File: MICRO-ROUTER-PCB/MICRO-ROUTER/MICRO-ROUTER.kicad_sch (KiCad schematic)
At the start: 71 parts, among them J2 USB_A, J3 USB_C_Receptacle_USB2.0_16P, J4 Battery Connector, J5 SPI Header, J6 GPIO Header, J7 RJ45 5-2301996-6, Q1 FS8205A, SW2 8Devices Reset, SW3 UART Reset, U1 TP4056, U2 XC9142B33DMR-G, U3 CP2102N-Axx-xQFN20, U4 DW01A, X1 142-0711-821

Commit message: -added extra charge LED -wired TP4056
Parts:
- added D3: LED Green, LED_SMD:LED_0603_1608Metric, symbol Device:LED
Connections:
- net at C4.2, D1.2 (A), D2.2 (A)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: now also D3.2 (A)
- net at D2.1 (K), R5.1: now also D3.1 (K)
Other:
- moved on the sheet: C4, D2
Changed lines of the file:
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@@
 	)
 	(junction
-		(at 146.05 110.49)
-		(diameter 0)
-		(color 0 0 0 0)
-	)
-	(junction
 		(at 133.35 110.49)
 		(diameter 0)
@@
 	)
 	(junction
+		(at 160.02 110.49)
+		(diameter 0)
+		(color 0 0 0 0)
+	)
+	(junction
 		(at 212.09 81.28)
 		(diameter 0)
@@
 	)
 	(junction
+		(at 151.13 93.98)
+		(diameter 0)
+		(color 0 0 0 0)
+	)
+	(junction
 		(at 180.34 212.09)
 		(diameter 0)
@@
 	)
 	(junction
+		(at 151.13 110.49)
+		(diameter 0)
+		(color 0 0 0 0)
+	)
+	(junction
 		(at 314.96 60.96)
 		(diameter 0)
@@
 	(wire
 		(pts
+			(xy 151.13 93.98) (xy 151.13 99.06)
+		)
+		(stroke
+			(width 0)
+			(type default)
+		)
+	)
+	(wire
+		(pts
 			(xy 323.85 113.03) (xy 326.39 113.03)
 		)
@@
 	(wire
 		(pts
-			(xy 146.05 99.06) (xy 146.05 93.98)
+			(xy 160.02 99.06) (xy 160.02 93.98)
 		)
 		(stroke
@@
 	(wire
 		(pts
+			(xy 151.13 93.98) (xy 160.02 93.98)
+		)
+		(stroke
+			(width 0)
+			(type default)
+		)
+	)
+	(wire
+		(pts
 			(xy 115.57 72.39) (xy 114.3 72.39)
 		)
@@
 	(wire
 		(pts
+			(xy 161.29 110.49) (xy 160.02 110.49)
+		)
+		(stroke
+			(width 0)
+			(type default)
+		)
+	)
+	(wire
+		(pts
 			(xy 99.06 83.82) (xy 102.87 83.82)
 		)
@@
 	(wire
 		(pts
+			(xy 151.13 93.98) (xy 146.05 93.98)
+		)
+		(stroke
+			(width 0)
+			(type default)
+		)
+	)
+	(wire
+		(pts
 			(xy 274.32 187.96) (xy 295.91 187.96)
 		)
@@
 	(wire
 		(pts
+			(xy 151.13 106.68) (xy 151.13 110.49)
+		)
+		(stroke
+			(width 0)
+			(type default)
+		)
+	)
+	(wire
+		(pts
 			(xy 171.45 219.71) (xy 190.5 219.71)
 		)
@@
 	(wire
 		(pts
-			(xy 146.05 106.68) (xy 146.05 110.49)
+			(xy 160.02 106.68) (xy 160.02 110.49)
 		)
 		(stroke
@@
 	(wire
 		(pts
-			(xy 146.05 110.49) (xy 139.7 110.49)
+			(xy 139.7 110.49) (xy 151.13 110.49)
 		)
 		(stroke
@@
 	(wire
 		(pts
+			(xy 151.13 110.49) (xy 160.02 110.49)
+		)
+		(stroke
+			(width 0)
+			(type default)
+		)
+	)
+	(wire
+		(pts
 			(xy 306.07 60.96) (xy 314.96 60.96)
 		)
@@
 	(symbol
 		(lib_id "power:GND")
-		(at 153.67 110.49 180)
+		(at 168.91 110.49 180)
 		(unit 1)
 		(exclude_from_sim no)
@@
 		(fields_autoplaced yes)
 		(property "Reference" "#PWR028"
-			(at 153.67 104.14 0)
+			(at 168.91 104.14 0)
 			(effects
 				(font
@@
 		)
 		(property "Value" "GND"
-			(at 153.67 105.41 0)
+			(at 168.91 105.41 0)
 			(effects
 				(font
@@
 		)
 		(property "Footprint" ""
-			(at 153.67 110.49 0)
+			(at 168.91 110.49 0)
 			(effects
 				(font
@@
 		)
 		(property "Datasheet" ""
-			(at 153.67 110.49 0)
+			(at 168.91 110.49 0)
 			(effects
 				(font
@@
 		)
 		(property "Description" "Power symbol creates a global label with name \"GND\" , ground"
-			(at 153.67 110.49 0)
+			(at 168.91 110.49 0)
 			(effects
 				(font
@@
 	)
 	(symbol
+		(lib_id "Device:LED")
+		(at 151.13 102.87 270)
+		(unit 1)
+		(exclude_from_sim no)
+		(in_bom yes)
+		(on_board yes)
+		(dnp no)
+		(property "Reference" "D3"
+			(at 150.876 105.664 90)
+			(effects
+				(font
+					(size 1.27 1.27)
+				)
+				(justify right)
+			)
+		)
+		(property "Value" "LED Green"
+			(at 153.924 105.918 0)
+			(effects
+				(font
+					(size 1.27 1.27)
+				)
+				(justify right)
+			)
+		)
+		(property "Footprint" "LED_SMD:LED_0603_1608Metric"
+			(at 151.13 102.87 0)
+			(effects
+				(font
+					(size 1.27 1.27)
+				)
+				(hide yes)
+			)
+		)
+		(property "Datasheet" "~"
+			(at 151.13 102.87 0)
+			(effects
+				(font
+					(size 1.27 1.27)
+				)
+				(hide yes)
+			)
+		)
+		(property "Description" "Light emitting diode"
+			(at 151.13 102.87 0)
+			(effects
+				(font
+					(size 1.27 1.27)
+				)
+				(hide yes)
+			)
+		)
+		(pin "1"
+		)
+		(pin "2"
+		)
+		(instances
+			(project "MICRO-ROUTER"
+				(path "/ebd99a91-a0ff-4b6f-9899-bd1b2d3fbcb2"
+					(reference "D3")
+					(unit 1)
+				)
+			)
+		)
+	)
+	(symbol
 		(lib_id "Device:R")
 		(at 146.05 90.17 180)
@@
 	(symbol
 		(lib_id "Device:C")
-		(at 149.86 110.49 270)
+		(at 165.1 110.49 270)
 		(unit 1)
 		(exclude_from_sim no)
@@
 		(dnp no)
 		(property "Reference" "C4"
-			(at 150.114 114.046 90)
+			(at 165.354 114.046 90)
 			(effects
 				(font
@@
 		)
 		(property "Value" "100nf"
-			(at 149.86 116.332 90)
+			(at 165.1 116.332 90)
 			(effects
 				(font
@@
 		)
 		(property "Footprint" "Capacitor_SMD:C_0603_1608Metric"
-			(at 146.05 111.4552 0)
+			(at 161.29 111.4552 0)
 			(effects
 				(font
@@
 		)
 		(property "Datasheet" "~"
-			(at 149.86 110.49 0)
+			(at 165.1 110.49 0)
 			(effects
 				(font
@@
 		)
 		(property "Description" "Unpolarized capacitor"
-			(at 149.86 110.49 0)
+			(at 165.1 110.49 0)
 			(effects
 				(font
@@
 	(symbol
 		(lib_id "Device:LED")
-		(at 146.05 102.87 270)
+		(at 160.02 102.87 270)
 		(unit 1)
 		(exclude_from_sim no)
@@
 		(dnp no)
 		(property "Reference" "D2"
-			(at 145.796 105.664 90)
+			(at 159.766 105.664 90)
 			(effects
 				(font
@@
 		)
 		(property "Value" "LED Green"
-			(at 148.844 105.918 0)
+			(at 162.814 105.918 0)
 			(effects
 				(font
@@
 		)
 		(property "Footprint" "LED_SMD:LED_0603_1608Metric"
-			(at 146.05 102.87 0)
+			(at 160.02 102.87 0)
 			(effects
 				(font
@@
 		)
 		(property "Datasheet" "~"
-			(at 146.05 102.87 0)
+			(at 160.02 102.87 0)
 			(effects
 				(font
@@
 		)
 		(property "Description" "Light emitting diode"
-			(at 146.05 102.87 0)
+			(at 160.02 102.87 0)
 			(effects
 				(font

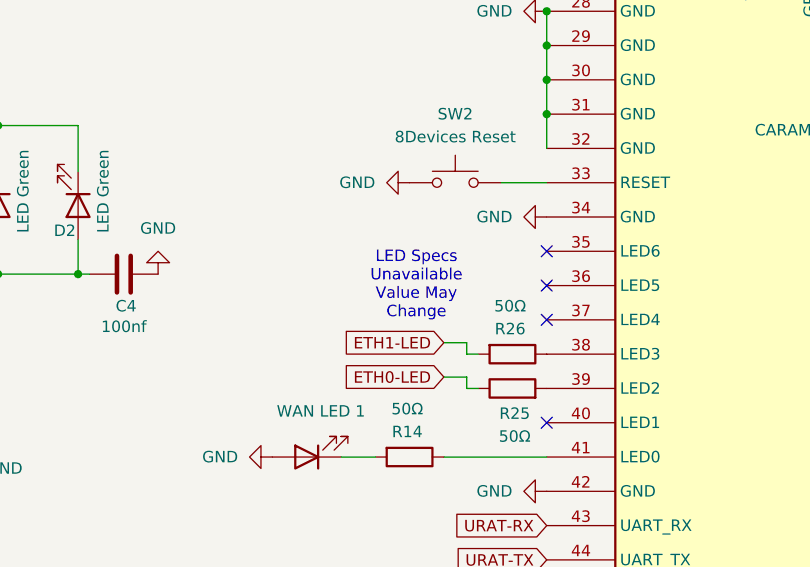
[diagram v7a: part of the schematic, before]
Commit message: -Wired up Mofset
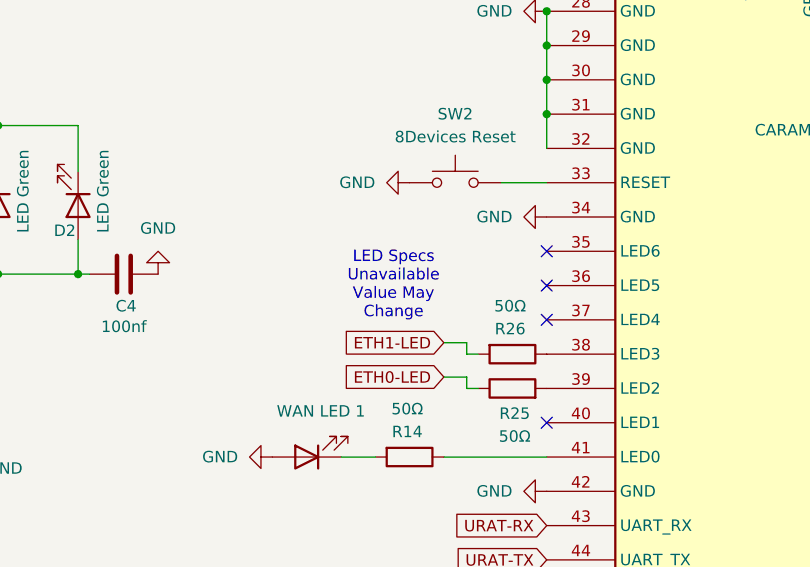
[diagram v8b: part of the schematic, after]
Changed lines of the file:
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@@
 	(text "LED Specs \nUnavailable\nValue May\nChange"
 		(exclude_from_sim no)
-		(at 197.612 111.76 0)
+		(at 195.072 111.76 0)
 		(effects
 			(font
